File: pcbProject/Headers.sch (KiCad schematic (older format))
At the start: 4 parts, among them P1 Power Header, P2 P2 Analog Header (AD), P3 Digital Header 02 (IOH) P3, P4 Digital Header 01 (IOL)

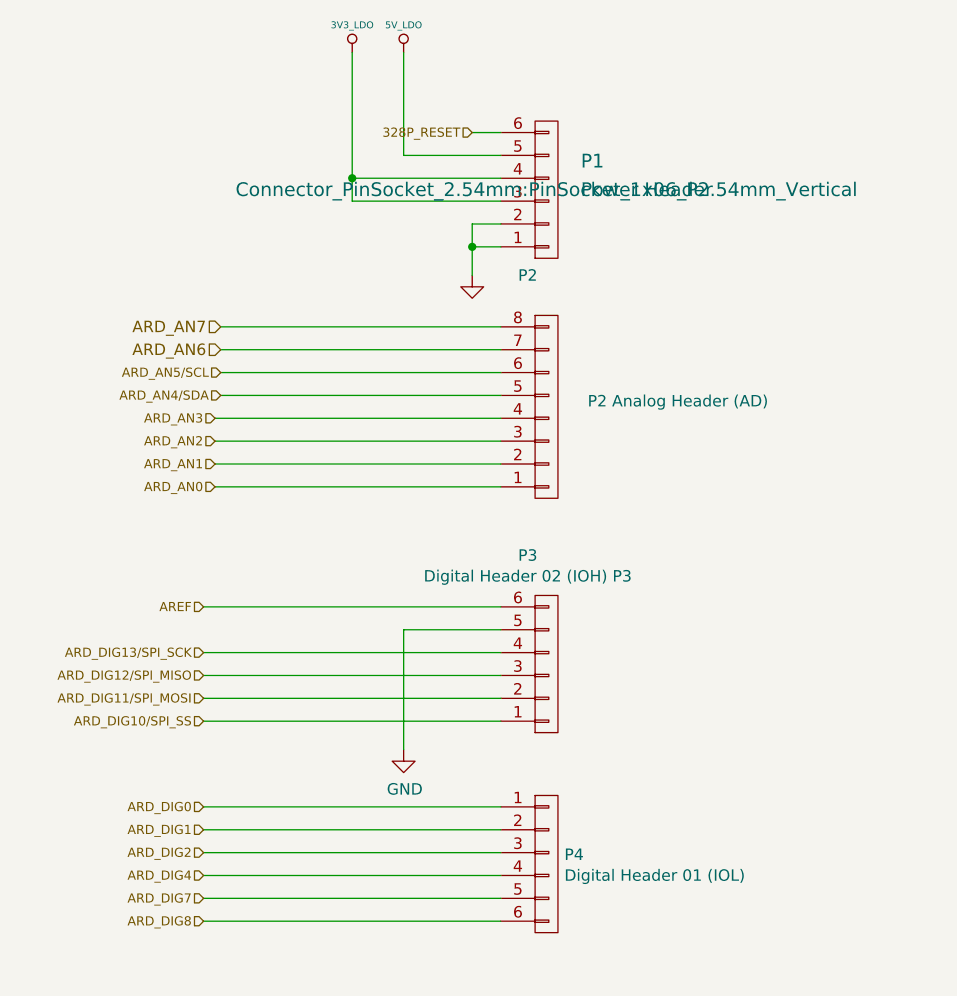
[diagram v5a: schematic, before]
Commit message: PCB versie3
Aanpassingen tips coach --> veel gewijzigd
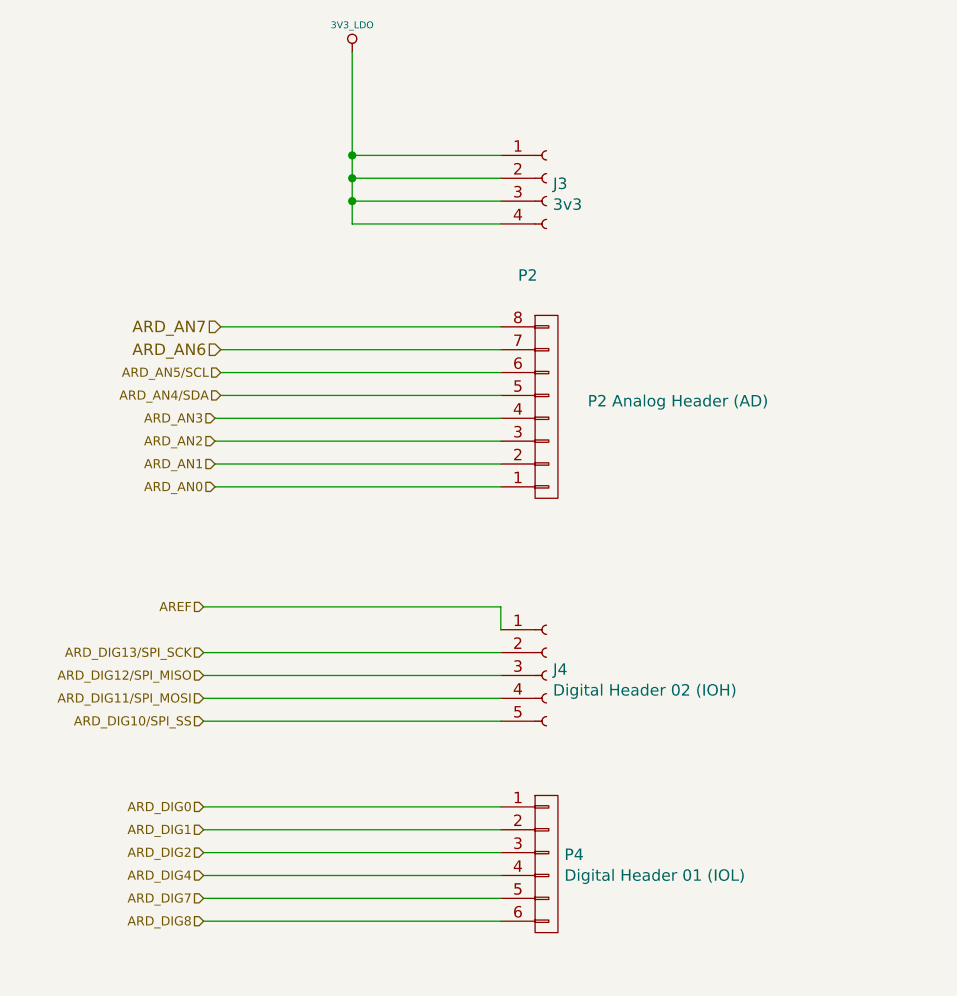
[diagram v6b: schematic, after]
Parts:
- removed P1: Power Header, Connector_PinSocket_2.54mm:PinSocket_1x06_P2.54mm_Vertical, symbol Arduino_Uno_R3_From_Scratch-rescue:CONN_01X06
- removed P3: Digital Header 02 (IOH) P3, Connector_PinSocket_2.54mm:PinSocket_1x06_P2.54mm_Vertical, symbol Arduino_Uno_R3_From_Scratch-rescue:CONN_01X06
- added J3: 3v3, Connector_PinSocket_2.54mm:PinSocket_1x04_P2.54mm_Vertical, symbol Connector:Conn_01x04_Female
- added J4: Digital Header 02 (IOH), Connector_PinSocket_2.54mm:PinSocket_1x05_P2.54mm_Vertical, symbol Connector:Conn_01x05_Female
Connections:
- net 3V3_LDO: now also J3.1 (Pin_1), J3.2 (Pin_2), J3.3 (Pin_3), J3.4 (Pin_4)
- net ARD_DIG10/SPI_SS: now also J4.5 (Pin_5)
- net ARD_DIG11/SPI_MOSI: now also J4.4 (Pin_4)
- net ARD_DIG12/SPI_MISO: now also J4.3 (Pin_3)
- net ARD_DIG13/SPI_SCK: now also J4.2 (Pin_2)
- net AREF: now also J4.1 (Pin_1)
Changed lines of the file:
@@
 $EndDescr
-$Comp
-L Arduino_Uno_R3_From_Scratch:5V_LDO #PWR035
-U 1 1 55E95D7A
-P 5625 1875
-F 0 "#PWR035" H 5625 1965 20  0001 C CNN
-F 1 "5V_LDO" H 5625 1995 30  0000 C CNN
-F 2 "~" H 5625 1875 60  0000 C CNN
-F 3 "~" H 5625 1875 60  0000 C CNN
-	1    5625 1875
-	1    0    0    -1
-$EndComp
 $Comp
 L Arduino_Uno_R3_From_Scratch:3V3_LDO #PWR036
@@
 	1    0    0    -1
 $EndComp
-Text HLabel 5925 2225 0    40   Input ~ 0
-328P_RESET
 Text HLabel 4800 3475 0    40   Input ~ 0
 ARD_AN3
@@
 Text HLabel 4750 4300 0    40   Input ~ 0
 AREF
-$Comp
-L Arduino_Uno_R3_From_Scratch-rescue:CONN_01X06 P1
-U 1 1 5C574D09
-P 6250 2475
-F 0 "P1" H 6400 2350 60  0000 L CNN
-F 1 "Power Header" H 6400 2475 60  0000 L CNN
-F 2 "Connector_PinSocket_2.54mm:PinSocket_1x06_P2.54mm_Vertical" H 6250 2475 60  0000 C CNN
-F 3 "http://sullinscorp.com/catalogs/101_PAGE114-115_.100_FEMALE_HDR.pdf" H 6250 2475 60  0001 C CNN
-F 4 "Connector Header 6 Position 0.100\" (2.54mm) Gold Surface Mount" H 6250 2475 60  0001 C CNN "Characteristics"
-F 5 "Shield Header 6POS - ANLG" H 6250 2475 60  0001 C CNN "Description"
-F 6 "Sullins Connector" H 6250 2475 60  0001 C CNN "MFN"
-F 7 "NPPC061KFXC-RC" H 6250 2475 60  0001 C CNN "MFP"
-F 8 "SMD" H 6250 2475 60  0001 C CNN "Package ID"
-F 9 "ANY" H 6250 2475 60  0001 C CNN "Source"
-F 10 "N" H 6250 2475 60  0001 C CNN "Critical"
-F 11 "Shield_Headers" H 6250 2475 60  0001 C CNN "Subsystem"
-F 12 "~" H 6250 2475 60  0001 C CNN "Notes"
-	1    6250 2475
-	1    0    0    1
-$EndComp
-$Comp
-L power:GND #PWR038
-U 1 1 55E9684A
-P 5925 2850
-F 0 "#PWR038" H 5925 2850 30  0001 C CNN
-F 1 "GND" H 5925 2780 30  0001 C CNN
-F 2 "~" H 5925 2850 60  0000 C CNN
-F 3 "~" H 5925 2850 60  0000 C CNN
-F 4 "ANY" H 5925 2850 60  0001 C CNN "Source"
-F 5 "N" H 5925 2850 60  0001 C CNN "Critical"
-F 6 "~" H 5925 2850 60  0001 C CNN "Notes"
-	1    5925 2850
-	1    0    0    -1
-$EndComp
-$Comp
-L power:GND #PWR0101
-U 1 1 5C579B64
-P 5625 4925
-F 0 "#PWR0101" H 5625 4675 50  0001 C CNN
-F 1 "GND" H 5630 4752 50  0000 C CNN
-F 2 "" H 5625 4925 50  0001 C CNN
-F 3 "" H 5625 4925 50  0001 C CNN
-	1    5625 4925
-	1    0    0    -1
-$EndComp
 Wire Wire Line
 	6050 4300 4750 4300
@@
 Wire Wire Line
 	4750 4700 6050 4700
-Wire Wire Line
-	6050 4400 5625 4400
-Wire Wire Line
-	5625 4400 5625 4925
-$Comp
-L Arduino_Uno_R3_From_Scratch-rescue:CONN_01X06 P3
-U 1 1 5C9A72A7
-P 6250 4550
-F 0 "P3" H 6168 4075 50  0000 C CNN
-F 1 "Digital Header 02 (IOH) P3" H 6168 4166 50  0000 C CNN
-F 2 "Connector_PinSocket_2.54mm:PinSocket_1x06_P2.54mm_Vertical" H 6250 4550 60  0001 C CNN
-F 3 "" H 6250 4550 60  0000 C CNN
-	1    6250 4550
-	1    0    0    1
-$EndComp
 $Comp
 L Arduino_Uno_R3_From_Scratch-rescue:CONN_01X06 P4
@@
 $EndComp
 Wire Wire Line
-	5925 2225 6050 2225
-Wire Wire Line
-	5925 2850 5925 2725
-Wire Wire Line
-	5925 2725 6050 2725
-Wire Wire Line
-	5925 2725 5925 2625
-Wire Wire Line
-	5925 2625 6050 2625
-Connection ~ 5925 2725
-Wire Wire Line
 	6050 2525 5400 2525
 Wire Wire Line
 	5400 2425 6050 2425
 Wire Wire Line
-	5400 1875 5400 2425
+	5400 1875 5400 2325
 Connection ~ 5400 2425
 Wire Wire Line
 	5400 2425 5400 2525
 Wire Wire Line
-	5625 1875 5625 2325
+	6050 2625 5400 2625
 Wire Wire Line
-	5625 2325 6050 2325
+	5400 2625 5400 2525
+Connection ~ 5400 2525
+$Comp
+L Connector:Conn_01x04_Female J3
+U 1 1 5C8FAAAF
+P 6250 2425
+F 0 "J3" H 6278 2401 50  0000 L CNN
+F 1 "3v3" H 6278 2310 50  0000 L CNN
+F 2 "Connector_PinSocket_2.54mm:PinSocket_1x04_P2.54mm_Vertical" H 6250 2425 50  0001 C CNN
+F 3 "~" H 6250 2425 50  0001 C CNN
+	1    6250 2425
+	1    0    0    -1
+$EndComp
+Wire Wire Line
+	6050 2325 5400 2325
+Connection ~ 5400 2325
+Wire Wire Line
+	5400 2325 5400 2425
+$Comp
+L Connector:Conn_01x05_Female J4
+U 1 1 5C8FCBE2
+P 6250 4600
+F 0 "J4" H 6278 4626 50  0000 L CNN
+F 1 "Digital Header 02 (IOH)" H 6278 4535 50  0000 L CNN
+F 2 "Connector_PinSocket_2.54mm:PinSocket_1x05_P2.54mm_Vertical" H 6250 4600 50  0001 C CNN
+F 3 "~" H 6250 4600 50  0001 C CNN
+	1    6250 4600
+	1    0    0    -1
+$EndComp
+Wire Wire Line
+	6050 4300 6050 4400
 $EndSCHEMATC

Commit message: verslag
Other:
- moved on the sheet: J3, P2
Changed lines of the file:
@@
 L Arduino_Uno_R3_From_Scratch:3V3_LDO #PWR036
 U 1 1 55E95D89
-P 5400 1875
-F 0 "#PWR036" H 5400 1835 30  0001 C CNN
-F 1 "3V3_LDO" H 5400 1995 30  0000 C CNN
-F 2 "~" H 5400 1875 60  0000 C CNN
-F 3 "~" H 5400 1875 60  0000 C CNN
-	1    5400 1875
+P 5700 2825
+F 0 "#PWR036" H 5700 2785 30  0001 C CNN
+F 1 "3V3_LDO" H 5700 2945 30  0000 C CNN
+F 2 "~" H 5700 2825 60  0000 C CNN
+F 3 "~" H 5700 2825 60  0000 C CNN
+	1    5700 2825
 	1    0    0    -1
 $EndComp
-Text HLabel 4800 3475 0    40   Input ~ 0
+Text HLabel 5850 3725 0    40   Input ~ 0
 ARD_AN3
-Text HLabel 4800 3575 0    40   Input ~ 0
+Text HLabel 5850 3825 0    40   Input ~ 0
 ARD_AN2
-Text HLabel 4800 3675 0    40   Input ~ 0
+Text HLabel 5850 3925 0    40   Input ~ 0
 ARD_AN1
-Text HLabel 4800 3775 0    40   Input ~ 0
+Text HLabel 5850 4025 0    40   Input ~ 0
 ARD_AN0
-Text HLabel 4750 5575 0    40   Input ~ 0
+Text HLabel 5850 5575 0    40   Input ~ 0
 ARD_DIG7
-Text HLabel 4750 5475 0    40   Input ~ 0
+Text HLabel 5850 5475 0    40   Input ~ 0
 ARD_DIG4
-Text HLabel 4750 5375 0    40   Input ~ 0
+Text HLabel 5850 5375 0    40   Input ~ 0
 ARD_DIG2
-Text HLabel 4750 5275 0    40   Input ~ 0
+Text HLabel 5850 5275 0    40   Input ~ 0
 ARD_DIG1
-Text HLabel 4750 5175 0    40   Input ~ 0
+Text HLabel 5850 5175 0    40   Input ~ 0
 ARD_DIG0
-Text HLabel 4825 3375 0    40   Input ~ 0
+Text HLabel 5875 3625 0    40   Input ~ 0
 ARD_AN4/SDA
-Text HLabel 4825 3275 0    40   Input ~ 0
+Text HLabel 5875 3525 0    40   Input ~ 0
 ARD_AN5/SCL
-Text HLabel 4750 5675 0    40   Input ~ 0
+Text HLabel 5850 5675 0    40   Input ~ 0
 ARD_DIG8
-Text HLabel 4750 4800 0    40   Input ~ 0
+Text HLabel 5850 4800 0    40   Input ~ 0
 ARD_DIG10/SPI_SS
-Text HLabel 4750 4700 0    40   Input ~ 0
+Text HLabel 5850 4700 0    40   Input ~ 0
 ARD_DIG11/SPI_MOSI
-Text HLabel 4750 4600 0    40   Input ~ 0
+Text HLabel 5850 4600 0    40   Input ~ 0
 ARD_DIG12/SPI_MISO
-Text HLabel 4750 4500 0    40   Input ~ 0
+Text HLabel 5850 4500 0    40   Input ~ 0
 ARD_DIG13/SPI_SCK
-Text HLabel 4750 4300 0    40   Input ~ 0
+Text HLabel 5850 4300 0    40   Input ~ 0
 AREF
-Wire Wire Line
-	6050 4300 4750 4300
-Wire Wire Line
-	6050 4500 4750 4500
-Wire Wire Line
-	6050 4600 4750 4600
 $Comp
 L Arduino_Uno_R3_From_Scratch-rescue:CONN_01X08 P2
 U 1 1 5C79CCDA
-P 6250 3425
-F 0 "P2" H 6168 2850 50  0000 C CNN
-F 1 "P2 Analog Header (AD)" H 6825 3400 50  0000 C CNN
-F 2 "Connector_PinSocket_2.54mm:PinSocket_1x08_P2.54mm_Vertical" H 6250 3425 60  0001 C CNN
-F 3 "" H 6250 3425 60  0000 C CNN
-	1    6250 3425
+P 6200 3675
+F 0 "P2" H 6118 3100 50  0000 C CNN
+F 1 "P2 Analog Header (AD)" H 6775 3650 50  0000 C CNN
+F 2 "Connector_PinSocket_2.54mm:PinSocket_1x08_P2.54mm_Vertical" H 6200 3675 60  0001 C CNN
+F 3 "" H 6200 3675 60  0000 C CNN
+	1    6200 3675
 	1    0    0    1
 $EndComp
-Wire Wire Line
-	4800 3775 6050 3775
-Wire Wire Line
-	4800 3675 6050 3675
-Wire Wire Line
-	4800 3575 6050 3575
-Wire Wire Line
-	4800 3475 6050 3475
-Wire Wire Line
-	4825 3375 6050 3375
-Wire Wire Line
-	4825 3275 6050 3275
-Text HLabel 4825 3175 0    50   Input ~ 0
+Text HLabel 5875 3425 0    50   Input ~ 0
 ARD_AN6
-Text HLabel 4825 3075 0    50   Input ~ 0
+Text HLabel 5875 3325 0    50   Input ~ 0
 ARD_AN7
-Wire Wire Line
-	4825 3175 6050 3175
-Wire Wire Line
-	4825 3075 6050 3075
-Wire Wire Line
-	4750 5175 6050 5175
-Wire Wire Line
-	4750 5275 6050 5275
-Wire Wire Line
-	4750 5375 6050 5375
-Wire Wire Line
-	4750 5475 6050 5475
-Wire Wire Line
-	4750 5575 6050 5575
-Wire Wire Line
-	4750 5675 6050 5675
-Wire Wire Line
-	4750 4800 6050 4800
-Wire Wire Line
-	4750 4700 6050 4700
 $Comp
 L Arduino_Uno_R3_From_Scratch-rescue:CONN_01X06 P4
@@
 	1    0    0    -1
 $EndComp
-Wire Wire Line
-	6050 2525 5400 2525
-Wire Wire Line
-	5400 2425 6050 2425
-Wire Wire Line
-	5400 1875 5400 2325
-Connection ~ 5400 2425
-Wire Wire Line
-	5400 2425 5400 2525
-Wire Wire Line
-	6050 2625 5400 2625
-Wire Wire Line
-	5400 2625 5400 2525
-Connection ~ 5400 2525
+Connection ~ 5925 2675
 $Comp
 L Connector:Conn_01x04_Female J3
 U 1 1 5C8FAAAF
-P 6250 2425
-F 0 "J3" H 6278 2401 50  0000 L CNN
-F 1 "3v3" H 6278 2310 50  0000 L CNN
-F 2 "Connector_PinSocket_2.54mm:PinSocket_1x04_P2.54mm_Vertical" H 6250 2425 50  0001 C CNN
-F 3 "~" H 6250 2425 50  0001 C CNN
-	1    6250 2425
+P 6200 2675
+F 0 "J3" H 6228 2651 50  0000 L CNN
+F 1 "3v3" H 6228 2560 50  0000 L CNN
+F 2 "Connector_PinSocket_2.54mm:PinSocket_1x04_P2.54mm_Vertical" H 6200 2675 50  0001 C CNN
+F 3 "~" H 6200 2675 50  0001 C CNN
+	1    6200 2675
 	1    0    0    -1
 $EndComp
 Wire Wire Line
-	6050 2325 5400 2325
-Connection ~ 5400 2325
-Wire Wire Line
-	5400 2325 5400 2425
+	5925 2575 5925 2675
 $Comp
 L Connector:Conn_01x05_Female J4
@@
 Wire Wire Line
 	6050 4300 6050 4400
+Wire Wire Line
+	5700 2825 5700 2875
+Wire Wire Line
+	5700 2875 5925 2875
+Wire Wire Line
+	5875 3325 6000 3325
+Wire Wire Line
+	5875 3425 6000 3425
+Wire Wire Line
+	5875 3525 6000 3525
+Wire Wire Line
+	5875 3625 6000 3625
+Wire Wire Line
+	5850 3725 6000 3725
+Wire Wire Line
+	5850 3825 6000 3825
+Wire Wire Line
+	5850 3925 6000 3925
+Wire Wire Line
+	5850 4025 6000 4025
+Wire Wire Line
+	5850 4300 6050 4300
+Wire Wire Line
+	5850 4500 6050 4500
+Wire Wire Line
+	5850 4600 6050 4600
+Wire Wire Line
+	5850 4700 6050 4700
+Wire Wire Line
+	5850 4800 6050 4800
+Wire Wire Line
+	5850 5175 6050 5175
+Wire Wire Line
+	5850 5275 6050 5275
+Wire Wire Line
+	5850 5375 6050 5375
+Wire Wire Line
+	5850 5475 6050 5475
+Wire Wire Line
+	5850 5575 6050 5575
+Wire Wire Line
+	5850 5675 6050 5675
+Wire Wire Line
+	5925 2675 5925 2775
+Wire Wire Line
+	5925 2575 6000 2575
+Wire Wire Line
+	5925 2675 6000 2675
+Wire Wire Line
+	5925 2775 6000 2775
+Connection ~ 5925 2775
+Wire Wire Line
+	5925 2775 5925 2875
+Wire Wire Line
+	5925 2875 6000 2875
+Connection ~ 5925 2875
 $EndSCHEMATC
